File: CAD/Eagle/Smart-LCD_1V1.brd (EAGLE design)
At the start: 99 x 67.7 mm, 54 parts, among them Q121 MMBT2222AL, U101 MEGA8-P, U221 MCP4018T-104E/LT, U401 TS4871ID, X131 LDR, X141 Switches, X151 LEDs, X201 LCD_23WAY__UC1608, X231 LED_A, X232 LED_K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

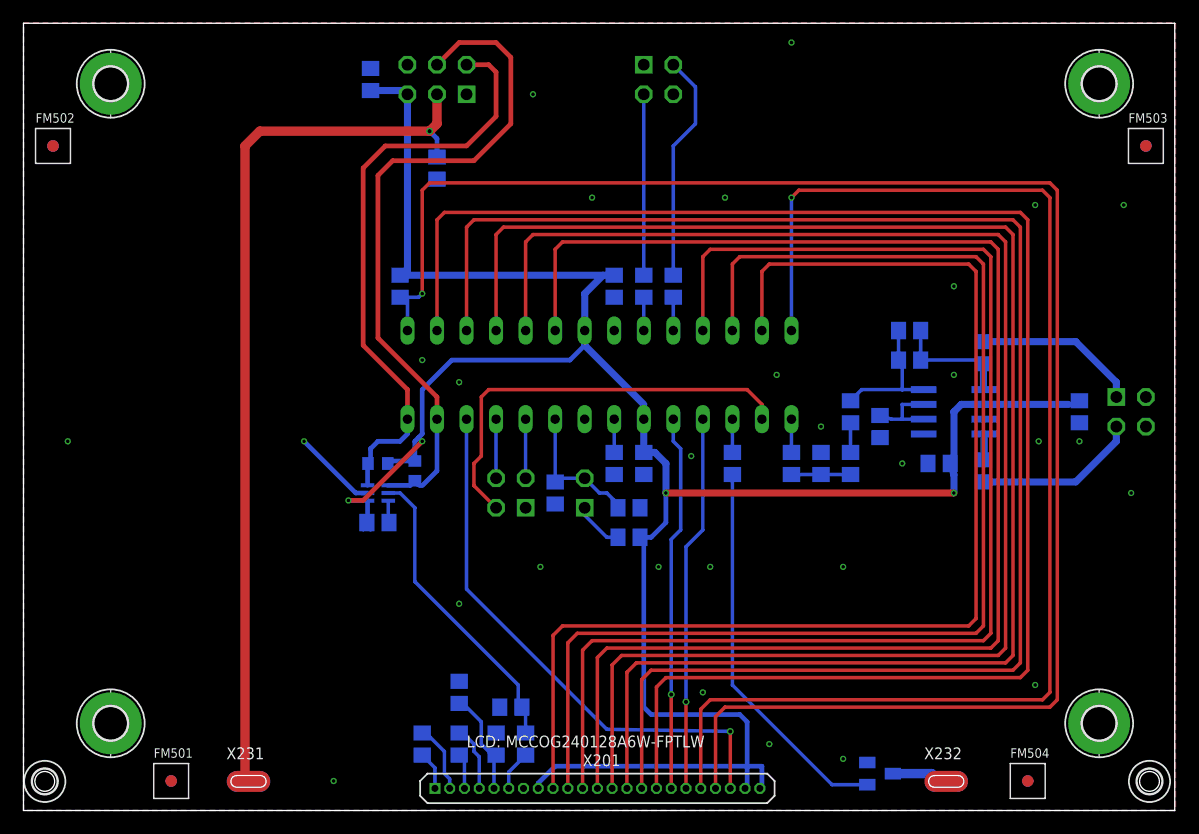
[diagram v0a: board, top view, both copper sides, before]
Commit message: HW_V1.1 - LCD backlight basis resistor chnaged to 4.7k ohms
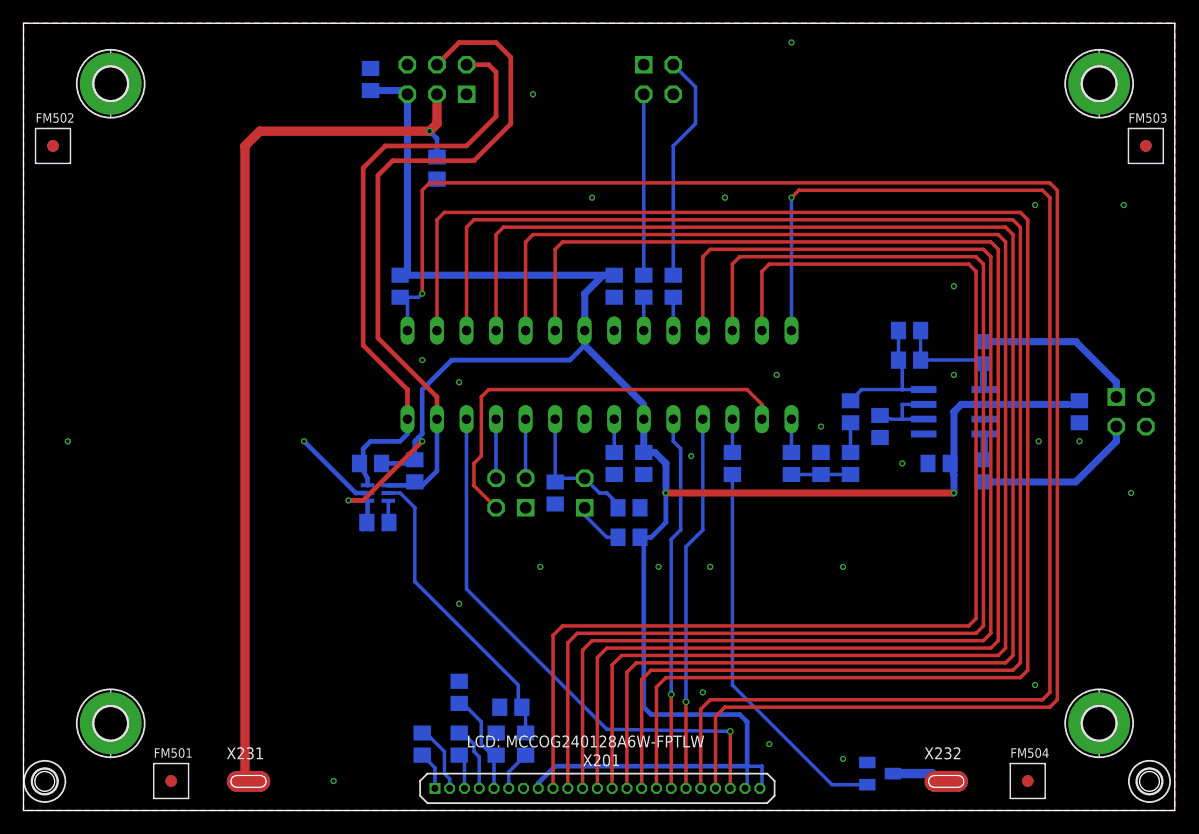
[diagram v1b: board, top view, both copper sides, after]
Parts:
- R121: value 18kR -> 4.7kR
- R391, R392: value 1.5kR -> 1kR; device rcl:R0603 -> rcl:R0805
- moved R391 0.64 mm to (29.8, 29.8)
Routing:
- net +3V3: track 201.7 -> 202.5 mm
- net SCL: track 51.3 -> 52.1 mm

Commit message: HW_V1.1 - photo diode - resistor change from 100k to 1MR
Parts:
- added D131: BZX84-C2V4, df4iah_diode:SOT23
- R131: value 33kR -> 27R
- R132: value 5.6kR -> 1MR
- moved R132 5.75 mm to (45.1, 21.6), turned to 180 degrees
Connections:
- net GND: now also D131.3, R132.1; no longer R132.2
- net LDR: now also D131.2, R132.2; no longer R132.1
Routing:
- net LDR: track 11.7 -> 21.1 mm
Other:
- board text added: "PhD"
- board text removed: "LDR"
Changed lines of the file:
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@@
 <setting verticaltext="up"/>
 </settings>
-<grid distance="0.05" unitdist="inch" unit="mm" style="lines" multiple="1" display="no" altdistance="0.025" altunitdist="inch" altunit="mm"/>
+<grid distance="0.05" unitdist="inch" unit="mm" style="lines" multiple="1" display="yes" altdistance="0.025" altunitdist="inch" altunit="mm"/>
 <layers>
 <layer number="1" name="Top" color="4" fill="1" visible="yes" active="yes"/>
@@
 <text x="27.94" y="62.865" size="1.4224" layer="22" ratio="15" rot="MR0">Smart-LCD V1.1
 by DF4IAH</text>
-<text x="48.26" y="22.86" size="1.016" layer="26" ratio="12" rot="MR0">LDR</text>
+<text x="48.895" y="22.86" size="1.016" layer="26" ratio="12" rot="MR0">PhD</text>
 <text x="38.1" y="5.43" size="1.016" layer="21" ratio="12">LCD: MCCOG240128A6W-FPTLW</text>
 <text x="36.83" y="58.42" size="1.016" layer="26" ratio="12" rot="MR0">I2C</text>
@@
 </class>
 </classes>
-<designrules name="Smart-LCD_1V1">
+<designrules name="Smart-LCD_1V1 *">
 <description language="de">
 &lt;p&gt;
@@
 <param name="mdWireWire" value="0.3mm"/>
 <param name="mdWirePad" value="0.5mm"/>
-<param name="mdWireVia" value="0.205mm"/>
-<param name="mdPadPad" value="0.205mm"/>
-<param name="mdPadVia" value="0.205mm"/>
-<param name="mdViaVia" value="0.205mm"/>
+<param name="mdWireVia" value="0.3mm"/>
+<param name="mdPadPad" value="0.3mm"/>
+<param name="mdPadVia" value="0.3mm"/>
+<param name="mdViaVia" value="0.3mm"/>
 <param name="mdSmdPad" value="0mil"/>
 <param name="mdSmdVia" value="0mil"/>
@@
 <attribute name="VALUE" x="48.26" y="27.94" size="0.6096" layer="28" rot="MR270"/>
 </element>
-<element name="R131" library="rcl" package="R0805" value="33kR" x="52.07" y="23.495" smashed="yes" rot="MR0">
+<element name="R131" library="rcl" package="R0805" value="27R" x="52.07" y="23.495" smashed="yes" rot="MR0">
 <attribute name="NAME" x="53.34" y="21.59" size="0.6096" layer="26" rot="MR0"/>
 <attribute name="VALUE" x="53.34" y="22.86" size="0.6096" layer="28" rot="MR0"/>
@@
 <attribute name="VALUE" x="74.93" y="41.275" size="0.6096" layer="28" rot="MR180"/>
 </element>
-<element name="R132" library="rcl" package="R0805" value="5.6kR" x="45.72" y="27.305" smashed="yes" rot="MR270">
-<attribute name="NAME" x="46.355" y="24.13" size="0.6096" layer="26" rot="MR0"/>
-<attribute name="VALUE" x="48.26" y="27.94" size="1.27" layer="28" rot="MR270"/>
+<element name="R132" library="rcl" package="R0805" value="1MR" x="45.085" y="21.59" smashed="yes" rot="MR180">
+<attribute name="NAME" x="49.53" y="20.955" size="0.6096" layer="26" rot="MR0"/>
+<attribute name="VALUE" x="44.45" y="24.13" size="1.27" layer="28" rot="MR180"/>
 </element>
 <element name="FM502" library="df4iah_fiducial" package="FIDUCIAL_MARK_1MM" value="FIDUCIAL_MARK_1MM" x="2.54" y="57.15" locked="yes"/>
@@
 <element name="FM503" library="df4iah_fiducial" package="FIDUCIAL_MARK_1MM" value="FIDUCIAL_MARK_1MM" x="96.52" y="57.15" locked="yes"/>
 <element name="FM504" library="df4iah_fiducial" package="FIDUCIAL_MARK_1MM" value="FIDUCIAL_MARK_1MM" x="86.36" y="2.54" locked="yes"/>
+<element name="D131" library="df4iah_diode" package="SOT23" value="BZX84-C2V4" x="46.99" y="18.415" smashed="yes" rot="MR90">
+<attribute name="NAME" x="43.815" y="17.78" size="0.6096" layer="26" rot="MR90"/>
+<attribute name="VALUE" x="43.815" y="16.51" size="1.27" layer="28" rot="MR90"/>
+</element>
 </elements>
 <signals>
@@
 <via x="64.135" y="5.715" extent="1-16" drill="0.3"/>
 <via x="37.465" y="17.78" extent="1-16" drill="0.3"/>
-<via x="44.45" y="20.955" extent="1-16" drill="0.3"/>
+<via x="50.165" y="17.78" extent="1-16" drill="0.3"/>
 <via x="54.61" y="20.955" extent="1-16" drill="0.3"/>
 <via x="59.055" y="20.955" extent="1-16" drill="0.3"/>
@@
 <via x="66.04" y="66.04" extent="1-16" drill="0.3"/>
 <via x="43.815" y="61.595" extent="1-16" drill="0.3"/>
-<contactref element="R132" pad="2"/>
+<contactref element="R132" pad="1"/>
+<contactref element="D131" pad="3"/>
 </signal>
 <signal name="+5V">
@@
 <signal name="LDR">
 <contactref element="C131" pad="1"/>
-<contactref element="X131" pad="2"/>
 <contactref element="U101" pad="23"/>
-<wire x1="45.72" y1="33.655" x2="45.72" y2="28.575" width="0.3048" layer="16"/>
-<wire x1="45.72" y1="28.575" x2="48.26" y2="28.575" width="0.3048" layer="16"/>
-<wire x1="48.26" y1="28.575" x2="49.53" y2="27.305" width="0.3048" layer="16"/>
 <wire x1="49.53" y1="27.305" x2="50.165" y2="27.305" width="0.3048" layer="16"/>
 <wire x1="50.165" y1="27.305" x2="50.8" y2="26.67" width="0.3048" layer="16"/>
 <wire x1="50.8" y1="26.67" x2="51.12" y2="26.035" width="0.3" layer="16"/>
-<contactref element="R132" pad="1"/>
-<wire x1="45.72" y1="28.255" x2="45.72" y2="28.575" width="0" layer="19" extent="16-16"/>
+<contactref element="R132" pad="2"/>
+<contactref element="X131" pad="2"/>
+<contactref element="D131" pad="2"/>
+<wire x1="49.53" y1="27.305" x2="48.26" y2="28.575" width="0.3048" layer="16"/>
+<wire x1="45.72" y1="33.655" x2="45.72" y2="28.575" width="0.3048" layer="16"/>
+<wire x1="45.72" y1="28.575" x2="45.72" y2="22.225" width="0.3048" layer="16"/>
+<wire x1="48.26" y1="28.575" x2="45.72" y2="28.575" width="0.3048" layer="16"/>
+<wire x1="45.72" y1="22.225" x2="45.808725" y2="22.136275" width="0.3048" layer="16"/>
+<wire x1="45.808725" y1="22.136275" x2="46.035" y2="21.59" width="0.3048" layer="16" curve="-45"/>
+<wire x1="45.89" y1="19.365" x2="45.72" y2="19.775415625" width="0.3048" layer="16" curve="-45"/>
+<wire x1="45.72" y1="19.775415625" x2="45.72" y2="20.955" width="0.3048" layer="16"/>
+<wire x1="45.72" y1="20.955" x2="45.808725" y2="21.043725" width="0.3048" layer="16"/>
+<wire x1="45.808725" y1="21.043725" x2="46.035" y2="21.59" width="0.3048" layer="16" curve="45"/>
 </signal>
 <signal name="LDR_P">

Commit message: HW_V1.1 - I2C poti removed
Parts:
- removed R222: 650kR, rcl:R0805
- removed U221: MCP4018T-104E/LT, df4iah_dig-pot:SOT65P210X110-6N
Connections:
- removed net POT_A: R222.1, U221.6
- net +3V3: no longer R222.2, U221.1
- net GND: no longer U221.2
- net POT_W: no longer U221.5
- net SCL: no longer U221.3
- net SDA: no longer U221.4
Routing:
- net GND: track 7.95 -> 0.65 mm, vias 29 -> 28
- net +3V3: track 202.5 -> 198.9 mm
- net POT_A: track 1.90 -> 0.00 mm
- net SDA: track 59.5 -> 57.6 mm
- net POT_W: track 26.1 -> 25.1 mm
- net SCL: track 52.1 -> 51.6 mm
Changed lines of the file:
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@@
 <layers>
 <layer number="1" name="Top" color="4" fill="1" visible="yes" active="yes"/>
-<layer number="2" name="Route2" color="1" fill="3" visible="yes" active="yes"/>
+<layer number="2" name="Route2" color="1" fill="3" visible="no" active="yes"/>
 <layer number="3" name="Route3" color="4" fill="3" visible="no" active="no"/>
 <layer number="14" name="Route14" color="1" fill="6" visible="no" active="no"/>
-<layer number="15" name="Route15" color="4" fill="6" visible="yes" active="yes"/>
+<layer number="15" name="Route15" color="4" fill="6" visible="no" active="yes"/>
 <layer number="16" name="Bottom" color="1" fill="1" visible="yes" active="yes"/>
 <layer number="17" name="Pads" color="2" fill="1" visible="yes" active="yes"/>
@@
 <layer number="29" name="tStop" color="7" fill="3" visible="yes" active="yes"/>
 <layer number="30" name="bStop" color="7" fill="6" visible="yes" active="yes"/>
-<layer number="31" name="tCream" color="7" fill="4" visible="yes" active="yes"/>
-<layer number="32" name="bCream" color="7" fill="5" visible="yes" active="yes"/>
+<layer number="31" name="tCream" color="7" fill="4" visible="no" active="yes"/>
+<layer number="32" name="bCream" color="7" fill="5" visible="no" active="yes"/>
 <layer number="33" name="tFinish" color="6" fill="3" visible="no" active="yes"/>
 <layer number="34" name="bFinish" color="6" fill="6" visible="no" active="yes"/>
@@
 <attribute name="VALUE" x="40.005" y="4.445" size="0.6096" layer="28" rot="MR90"/>
 </element>
-<element name="R222" library="rcl" package="R0805" value="650kR" x="30.48" y="24.765" smashed="yes" rot="MR0">
-<attribute name="NAME" x="31.75" y="22.86" size="0.6096" layer="26" rot="MR0"/>
-<attribute name="VALUE" x="31.75" y="24.13" size="0.6096" layer="28" rot="MR0"/>
-</element>
 <element name="R221" library="rcl" package="R0805" value="100kR" x="43.18" y="5.715" smashed="yes" rot="MR270">
 <attribute name="NAME" x="44.45" y="4.445" size="0.6096" layer="26" rot="MR90"/>
@@
 <attribute name="NAME" x="43.18" y="10.16" size="0.6096" layer="26" rot="MR0"/>
 <attribute name="VALUE" x="43.18" y="8.255" size="0.6096" layer="28" rot="MR0"/>
-</element>
-<element name="U221" library="df4iah_dig-pot" package="SOT65P210X110-6N" value="MCP4018T-104E/LT" x="30.48" y="27.305" smashed="yes" rot="MR180">
-<attribute name="MPN" value="MCP4018T-104E/LT" x="30.48" y="27.305" size="1.016" layer="28" rot="MR180" display="off"/>
-<attribute name="OC_FARNELL" value="1825018" x="30.48" y="27.305" size="1.016" layer="28" rot="MR180" display="off"/>
-<attribute name="OC_NEWARK" value="08R1802" x="30.48" y="27.305" size="1.016" layer="28" rot="MR180" display="off"/>
-<attribute name="PACKAGE" value="SOT-6" x="30.48" y="27.305" size="1.016" layer="28" rot="MR180" display="off"/>
-<attribute name="SUPPLIER" value="Microchip" x="30.48" y="27.305" size="1.016" layer="28" rot="MR180" display="off"/>
-<attribute name="NAME" x="34.925" y="26.67" size="0.6096" layer="26" ratio="10" rot="SMR0"/>
-<attribute name="VALUE" x="42.2148" y="23.749" size="0.6096" layer="28" ratio="10" rot="SMR0"/>
 </element>
 <element name="C302" library="rcl" package="C0805" value="100nF" x="29.845" y="62.865" smashed="yes" rot="MR90">
@@
 <element name="R132" library="rcl" package="R0805" value="1MR" x="45.085" y="21.59" smashed="yes" rot="MR180">
 <attribute name="NAME" x="49.53" y="20.955" size="0.6096" layer="26" rot="MR0"/>
-<attribute name="VALUE" x="44.45" y="24.13" size="1.27" layer="28" rot="MR180"/>
+<attribute name="VALUE" x="39.37" y="21.59" size="0.6096" layer="28" rot="MR180"/>
 </element>
 <element name="FM502" library="df4iah_fiducial" package="FIDUCIAL_MARK_1MM" value="FIDUCIAL_MARK_1MM" x="2.54" y="57.15" locked="yes"/>
@@
 <element name="D131" library="df4iah_diode" package="SOT23" value="BZX84-C2V4" x="46.99" y="18.415" smashed="yes" rot="MR90">
 <attribute name="NAME" x="43.815" y="17.78" size="0.6096" layer="26" rot="MR90"/>
-<attribute name="VALUE" x="43.815" y="16.51" size="1.27" layer="28" rot="MR90"/>
+<attribute name="VALUE" x="43.815" y="16.51" size="0.6096" layer="28" rot="MR90"/>
 </element>
 </elements>
@@
 <contactref element="C302" pad="2"/>
 <contactref element="C221" pad="2"/>
-<contactref element="U221" pad="2"/>
 <contactref element="X201" pad="7"/>
 <contactref element="R211" pad="1"/>
@@
 <via x="48.895" y="52.705" extent="1-16" drill="0.3"/>
 <via x="60.325" y="52.705" extent="1-16" drill="0.3"/>
-<via x="24.13" y="31.75" extent="1-16" drill="0.3"/>
-<wire x1="29.591" y1="27.305" x2="28.575" y2="27.305" width="0.4064" layer="16"/>
-<wire x1="28.575" y1="27.305" x2="24.13" y2="31.75" width="0.4064" layer="16"/>
 <via x="26.67" y="2.54" extent="1-16" drill="0.3"/>
 <via x="70.485" y="4.445" extent="1-16" drill="0.3"/>
@@
 <contactref element="C102" pad="1"/>
 <contactref element="X201" pad="8"/>
-<contactref element="U221" pad="1"/>
-<contactref element="R222" pad="2"/>
-<wire x1="29.53" y1="24.765" x2="29.591" y2="24.826" width="0.3048" layer="16"/>
-<wire x1="29.591" y1="24.826" x2="29.591" y2="26.6446" width="0.4064" layer="16"/>
 <contactref element="R131" pad="1"/>
-<wire x1="29.845" y1="24.13" x2="29.845" y2="24.765" width="0.3" layer="16"/>
-<wire x1="29.845" y1="24.765" x2="29.53" y2="24.765" width="0.3" layer="16"/>
 <contactref element="R101" pad="1"/>
 <contactref element="U101" pad="20"/>
@@
 <contactref element="X201" pad="22"/>
 <contactref element="X201" pad="23"/>
-<wire x1="29.5656" y1="26.67" x2="29.591" y2="26.6446" width="0.3" layer="16"/>
 <wire x1="62.05" y1="1.905" x2="62.23" y2="1.905" width="0.3" layer="16"/>
 <wire x1="62.23" y1="1.905" x2="62.23" y2="3.81" width="0.3048" layer="16"/>
@@
 <wire x1="63.5" y1="3.81" x2="62.23" y2="3.81" width="0.3048" layer="16"/>
 <wire x1="62.23" y1="3.81" x2="62.23" y2="7.62" width="0.4064" layer="16"/>
-<wire x1="29.21" y1="24.13" x2="29.21" y2="24.445" width="0.3" layer="16"/>
-<wire x1="29.21" y1="24.445" x2="29.53" y2="24.765" width="0.4064" layer="16"/>
 <contactref element="U401" pad="6"/>
 <contactref element="C402" pad="1"/>
@@
 <contactref element="X301" pad="2"/>
 <contactref element="R391" pad="1"/>
-<contactref element="U221" pad="3"/>
 <wire x1="29.591" y1="28.536" x2="28.895" y2="29.845" width="0.4064" layer="16"/>
 <contactref element="U101" pad="28"/>
-<wire x1="29.591" y1="27.9654" x2="29.591" y2="28.536" width="0.4064" layer="16"/>
 <wire x1="29.21" y1="31.115" x2="29.21" y2="30.06" width="0.4064" layer="16"/>
 <wire x1="29.21" y1="30.06" x2="28.895" y2="29.845" width="0.4064" layer="16"/>
@@
 <contactref element="X301" pad="4"/>
 <contactref element="R392" pad="1"/>
-<contactref element="U221" pad="4"/>
 <contactref element="U101" pad="27"/>
 <wire x1="33.8954" y1="27.9654" x2="33.655" y2="28.26" width="0.3" layer="16"/>
-<wire x1="31.369" y1="27.9654" x2="33.2604" y2="27.9654" width="0.4064" layer="16"/>
 <wire x1="33.2604" y1="27.9654" x2="33.655" y2="28.26" width="0.4064" layer="16"/>
 <wire x1="35.56" y1="33.655" x2="35.56" y2="29.21" width="0.4064" layer="16"/>
@@
 <wire x1="35.38" y1="3.675" x2="34.29" y2="4.765" width="0.3048" layer="16"/>
 </signal>
-<signal name="POT_A">
-<contactref element="R222" pad="1"/>
-<contactref element="U221" pad="6"/>
-<wire x1="31.43" y1="24.765" x2="31.369" y2="24.826" width="0.3048" layer="16"/>
-<wire x1="31.369" y1="24.826" x2="31.369" y2="26.6446" width="0.3048" layer="16"/>
-</signal>
 <signal name="POT_W">
 <contactref element="C221" pad="1"/>
 <contactref element="R221" pad="1"/>
-<contactref element="U221" pad="5"/>
 <wire x1="43.18" y1="6.665" x2="43.18" y2="8.57" width="0.3048" layer="16"/>
 <wire x1="43.18" y1="8.57" x2="42.86" y2="8.89" width="0.3048" layer="16"/>
-<wire x1="31.369" y1="27.305" x2="32.385" y2="27.305" width="0.3048" layer="16"/>
 <wire x1="32.385" y1="27.305" x2="33.655" y2="26.035" width="0.3048" layer="16"/>
 <wire x1="33.655" y1="26.035" x2="33.655" y2="19.685" width="0.3048" layer="16"/>

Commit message: HW_V1.1 - suggestions of Hans, DK1NB added
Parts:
- R132: value 1MR -> 270kR
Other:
- board text added: "X131-1 = SFH203, cathode X131-2 = SFH203, anode"
- board text added: "X141-1 = GND X141-2 = RotEnc-I X141-3 = PushBut X141-4 = RotEnc-Q"
- board text added: "X151-1 = GND, LED cathodes X151-2 = LED red, anode X151-3 = LED green, anode"
- board text added: "X301-1 = GND X301-2 = SCL X301-3 = VCC 5.0V X301-4 = SDA X301-5 = VCC 3.3V X301-6 = GND"
- board text added: "X411-1 = Spk left + (8 ohms) X411-2 = Spk left - (8 ohms) X411-3 = N.C. X411-4 = N.C."
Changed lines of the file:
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@@
 <text x="49.53" y="24.13" size="0.6096" layer="22" ratio="20" rot="MR0">1</text>
 <text x="43.815" y="24.13" size="0.6096" layer="22" ratio="20" rot="MR0">1</text>
+<text x="83.82" y="60.96" size="1.016" layer="22" rot="MR0">X151-1 = GND, LED cathodes
+X151-2 = LED red,   anode
+X151-3 = LED green, anode</text>
+<text x="25.4" y="26.67" size="1.016" layer="22" rot="MR0">X131-1 = SFH203, cathode
+X131-2 = SFH203, anode</text>
+<text x="25.4" y="48.26" size="1.016" layer="22" rot="MR0">X301-1 = GND
+X301-2 = SCL
+X301-3 = VCC 5.0V
+X301-4 = SDA
+X301-5 = VCC 3.3V
+X301-6 = GND</text>
+<text x="25.4" y="17.78" size="1.016" layer="22" rot="MR0">X141-1 = GND
+X141-2 = RotEnc-I
+X141-3 = PushBut
+X141-4 = RotEnc-Q</text>
+<text x="96.52" y="17.78" size="1.016" layer="22" rot="MR0">X411-1 = Spk left +  (8 ohms)
+X411-2 = Spk left -  (8 ohms)
+X411-3 = N.C.
+X411-4 = N.C.</text>
 </plain>
 <attributes>
@@
 <attribute name="VALUE" x="74.93" y="41.275" size="0.6096" layer="28" rot="MR180"/>
 </element>
-<element name="R132" library="rcl" package="R0805" value="1MR" x="45.085" y="21.59" smashed="yes" rot="MR180">
+<element name="R132" library="rcl" package="R0805" value="270kR" x="45.085" y="21.59" smashed="yes" rot="MR180">
 <attribute name="NAME" x="49.53" y="20.955" size="0.6096" layer="26" rot="MR0"/>
 <attribute name="VALUE" x="39.37" y="21.59" size="0.6096" layer="28" rot="MR180"/>
